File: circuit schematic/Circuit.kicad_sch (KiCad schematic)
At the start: 20 parts

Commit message: Updated schematics
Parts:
- removed C?: 12nF, symbol pspice:CAP
- removed SB0, SB1: SW_Push, symbol Switch:SW_Push
- added C1: 12nF, symbol Device:C
- added D1: LED, symbol Device:LED
- added R6: 10K, symbol Device:R
- added R7: 1K, symbol Device:R
- added SB1 (x2): SW_Push, symbol Switch:SW_Push
- R1: renamed from R?; value 10kohm -> 10K
- R2, R3: renamed from R?; value 640ohm -> 640R
- R4: renamed from R?; value 220ohm -> 220R
- R5: renamed from R?; value 100ohm -> 100R
- gave numbers to parts that had none: 6
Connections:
- net +3.3V: now also R6.2, R7.1
- net GND: now also BT1.2 (-), U1.27 (GND), C1.2, D1.1 (K), SB1.2, SB1.2
- net LED_G: now reaches U1.31 (34_A15_RX5_CAN1RX_SDA0)
- net LED_G: now also R2.2; no longer R3.2
- net LIGHT_SENSE: now reaches R0.1, R1.1, U1.32 (35_A16_PWM)
- net LIGHT_SENSE: now also C1.1
- net D4: now reaches DS1.11 (D4), U1.4 (2_PWM)
- net D5: now reaches DS1.12 (D5), U1.5 (3_PWM_CAN0TX_SCL2)
- net D6: now reaches DS1.13 (D6), U1.6 (4_PWM_CAN0RX_SDA2)
- net D7: now reaches DS1.14 (D7), U1.7 (5_PWM_TX1_MISO1)
- net BACKLIGHT: now reaches DS1.15 (LED(+)), U1.33 (36_A17_PWM)
- net +5V: now reaches DS1.2 (VDD), U1.53 (Vin)
- net RS: now reaches DS1.4 (RS), U1.3 (1_TX1_MISO1_Touch)
- net E: now reaches DS1.6 (E), U1.2 (0_RX1_MOSI1_Touch)
- net SW_BB: now reaches BB.1, U1.41 (14_A0_PWM_SCK0)
- net LED_R: now reaches U1.30 (33_A14_TX5_CAN1TX_SCL0)
- net LED_R: now also R3.2; no longer R2.2
- net SW_LB: now reaches LB.1, U1.47 (20_A6_PWM_CS0_SCK1)
- net SW_SB0: now reaches U1.46 (19_A5_SCL0_Touch)
- net SW_SB0: now also SB1.1
- net SW_SB4: now reaches SB4.1, U1.42 (15_A1_CS0_Touch)
- net SW_SB3: now reaches SB3.1, U1.43 (16_A2_SCL0_Touch)
- net +BATT: now reaches SW1.1 (A)
- net +BATT: now also U1.25 (VBat)
- net at SW1.3 (C): no longer U1.25 (VBat)
- net SW_SB2: now reaches SB2.1, U1.44 (17_A3_SDA0_Touch)
- net SW_SB1: now reaches U1.45 (18_A4_SDA0_Touch)
- net SW_SB1: now also SB1.1
- net TEMP_SENSE: now reaches U1.8 (6_PWM), U?.2 (IO)
- net TEMP_SENSE: now also R6.1
- new net: D1.2 (A), R7.2
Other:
- title: (none) -> Sleep Monitor
- moved on the sheet: BB, LB, SB4

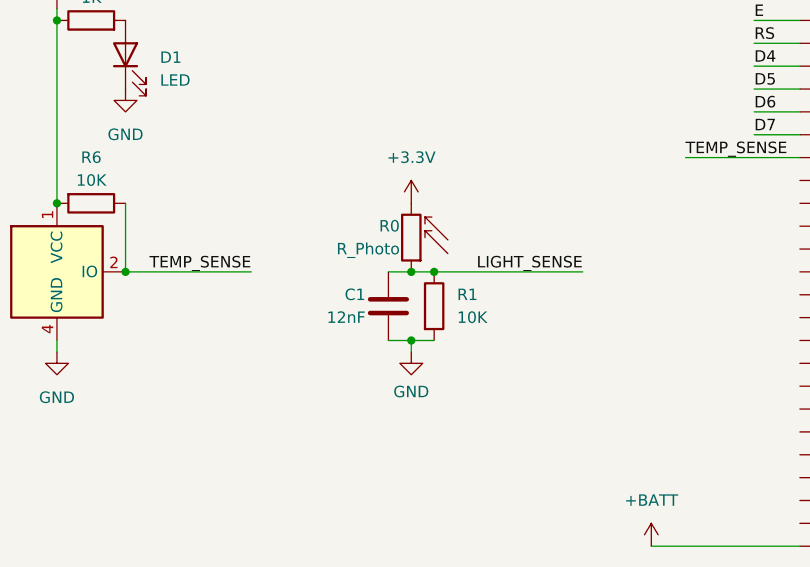
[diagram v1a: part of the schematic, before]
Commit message: Light sensing measurement improvements, schematic fixes
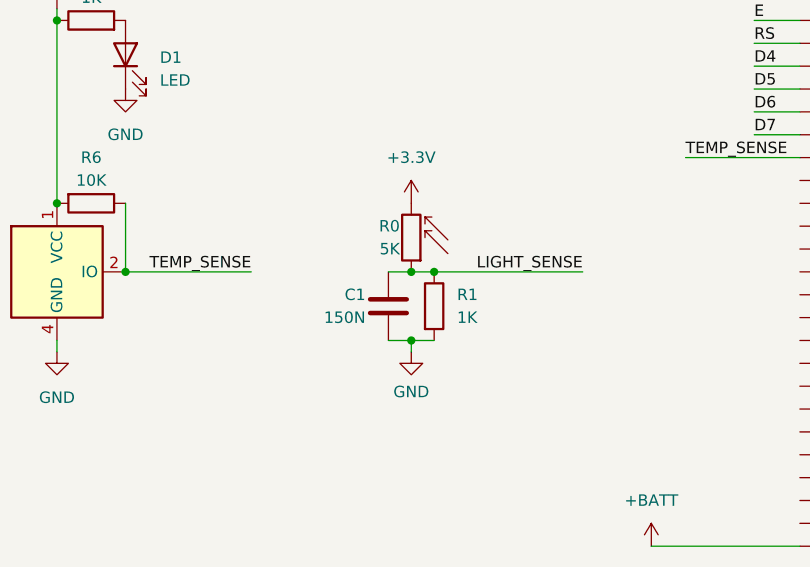
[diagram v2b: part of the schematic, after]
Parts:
- C1: value 12nF -> 150N
- R0: value R_Photo -> 5K
- R1: value 10K -> 1K
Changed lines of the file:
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@@
       (effects (font (size 1.27 1.27)) (justify right))
     )
-    (property "Value" "12nF" (id 1) (at 148.59 76.2 0)
+    (property "Value" "150N" (id 1) (at 148.59 76.2 0)
       (effects (font (size 1.27 1.27)) (justify right))
     )
@@
       (effects (font (size 1.27 1.27)) (justify left))
     )
-    (property "Value" "10K" (id 1) (at 158.75 76.2 0)
+    (property "Value" "1K" (id 1) (at 158.75 76.2 0)
       (effects (font (size 1.27 1.27)) (justify left))
     )
@@
       (effects (font (size 1.27 1.27)) (justify left))
     )
-    (property "Value" "R_Photo" (id 1) (at 152.4 68.58 0)
+    (property "Value" "5K" (id 1) (at 152.4 68.58 0)
       (effects (font (size 1.27 1.27)) (justify left))
     )
@@
     )
     (path "/31bc59c1-557f-4297-a5a8-395f00864f6f"
-      (reference "C1") (unit 1) (value "12nF") (footprint "")
+      (reference "C1") (unit 1) (value "150N") (footprint "")
     )
     (path "/4a8bf6e1-ec1c-453e-bde6-002c614c4299"
@@
     )
     (path "/ff8fe31f-0ec9-4426-89b1-0ee4d070bf6f"
-      (reference "R0") (unit 1) (value "R_Photo") (footprint "")
+      (reference "R0") (unit 1) (value "5K") (footprint "")
     )
     (path "/4089ab65-ea0c-4b85-b5b8-71733e0c4771"
-      (reference "R1") (unit 1) (value "10K") (footprint "")
+      (reference "R1") (unit 1) (value "1K") (footprint "")
     )
     (path "/838d8e57-d240-46d7-a070-ebe73b09ea82"
